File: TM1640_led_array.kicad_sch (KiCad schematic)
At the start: 50 parts, among them J1 TYPE-C-31-M-12, J2 3v3_H, J3 5v_H, Q1 NMOS, Q2 NMOS, Q3 NMOS, Q4 NMOS

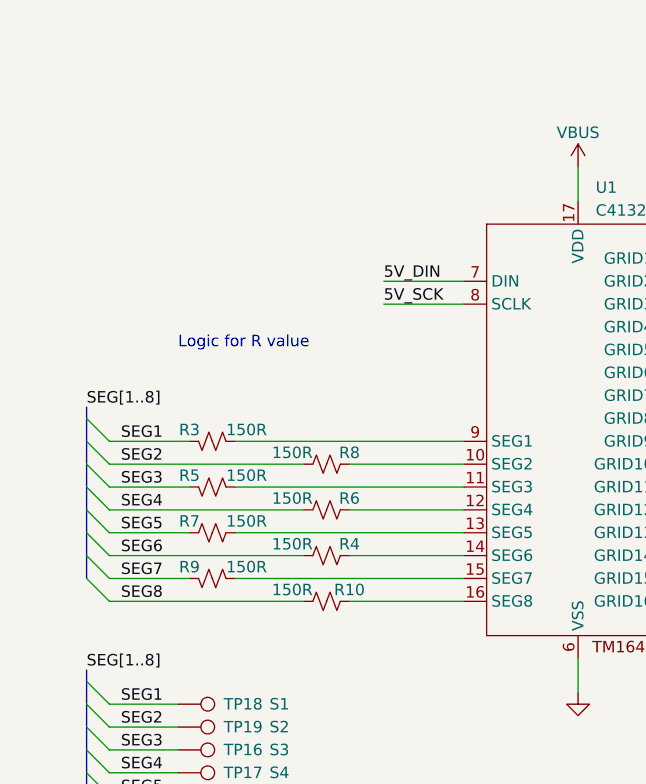
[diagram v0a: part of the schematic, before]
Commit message: added filter caps for driver chip to schematic
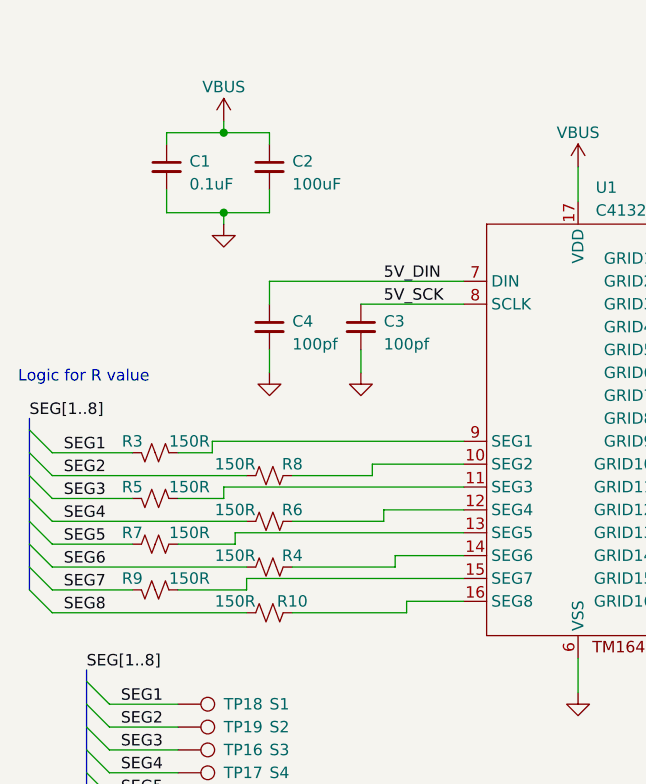
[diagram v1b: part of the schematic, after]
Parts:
- added C1: 0.1uF, Capacitor_SMD:C_0402_1005Metric, symbol Device:C_Small
- added C2: 100uF, Capacitor_SMD:C_1206_3216Metric, symbol Device:C_Small
- added C3, C4: 100pf, Capacitor_SMD:C_0402_1005Metric, symbol Device:C_Small
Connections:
- net 5V_DIN: now also C4.1
- net 5V_SCK: now also C3.1
- net GND: now also C1.2, C2.2, C3.2, C4.2
- net VBUS: now also C1.1, C2.1
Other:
- moved on the sheet: R10, R3, R4, R5, R6, R7, R8, R9
